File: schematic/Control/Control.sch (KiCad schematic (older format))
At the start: 0 parts

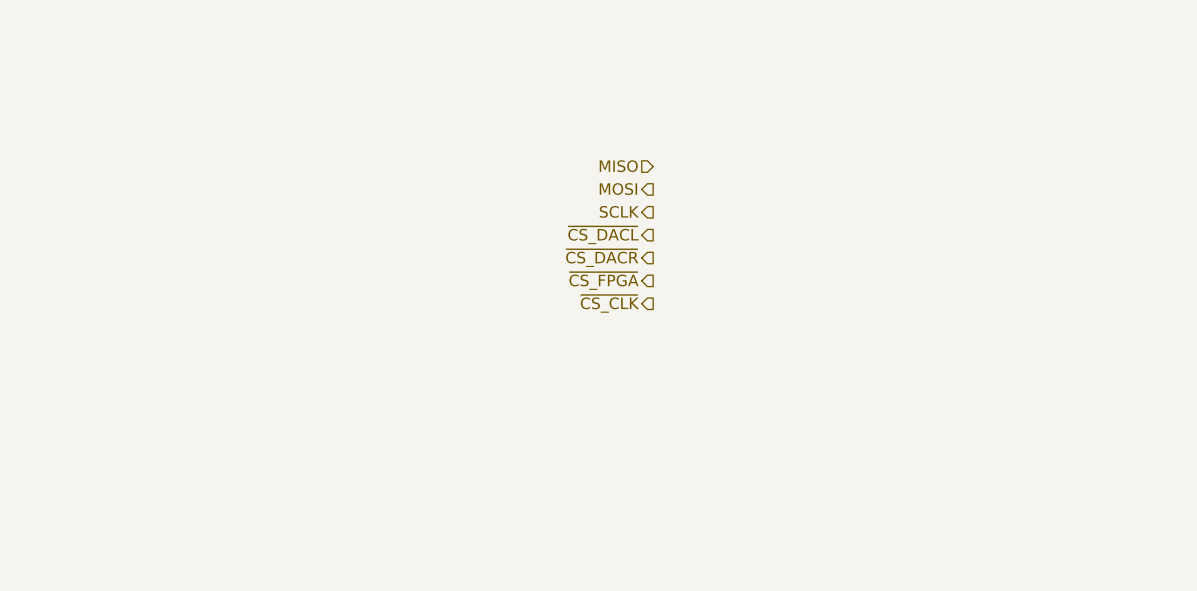
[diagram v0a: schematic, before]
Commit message: Control board diagram complete at high level - Clock, USB, Control, Power and IO done. Remaining is FPGA pin assignment which will be done later to optimize board layout.
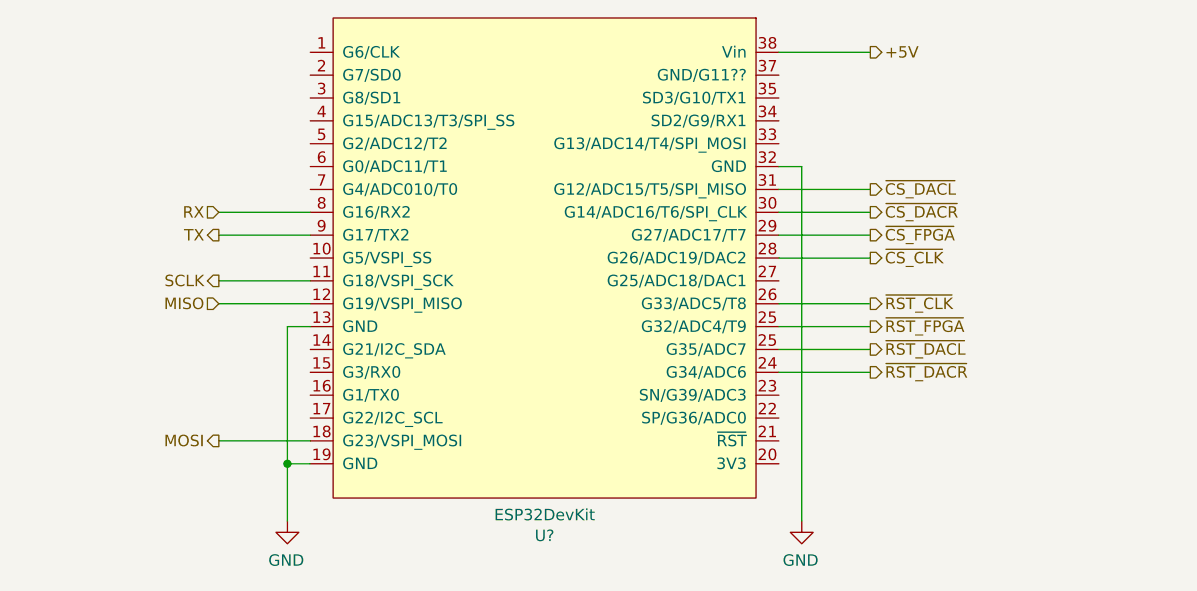
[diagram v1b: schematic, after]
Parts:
- added U?: ESP32DevKit, Zmei_Footprints:ESP32DevKit, symbol Zmei_elements:ESP32DevKit
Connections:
- net MISO: now also U?.12 (G19/VSPI_MISO)
- net MOSI: now also U?.18 (G23/VSPI_MOSI)
- net SCLK: now also U?.11 (G18/VSPI_SCK)
- net ~CS_CLK~: now also U?.28 (G26/ADC19/DAC2)
- net ~CS_DACL~: now also U?.31 (G12/ADC15/T5/SPI_MISO)
- net ~CS_DACR~: now also U?.30 (G14/ADC16/T6/SPI_CLK)
- net ~CS_FPGA~: now also U?.29 (G27/ADC17/T7)
- new net +5V: U?.38 (Vin)
- new net GND: U?.13 (GND), U?.19 (GND), U?.32 (GND)
- new net RX: U?.8 (G16/RX2)
- new net TX: U?.9 (G17/TX2)
- new net ~RST_CLK~: U?.26 (G33/ADC5/T8)
- new net ~RST_DACL~: U?.25 (G35/ADC7)
- new net ~RST_DACR~: U?.24 (G34/ADC6)
- new net ~RST_FPGA~: U?.25 (G35/ADC7)
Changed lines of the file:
@@
 EESchema Schematic File Version 4
-LIBS:DeWille-cache
 EELAYER 30 0
 EELAYER END
 $Descr A4 11693 8268
 encoding utf-8
-Sheet 4 7
+Sheet 3 5
 Title ""
 Date ""
@@
 Comment4 ""
 $EndDescr
-Text HLabel 6550 3600 0    50   Input ~ 0
+Text HLabel 7500 3700 2    50   Output ~ 0
+~CS_DACL~
+Text HLabel 7500 3800 2    50   Output ~ 0
+~CS_DACR~
+Text HLabel 7500 3900 2    50   Output ~ 0
+~CS_FPGA~
+Text HLabel 7500 4000 2    50   Output ~ 0
+~CS_CLK~
+Text HLabel 7500 4200 2    50   Output ~ 0
+~RST_CLK~
+Text HLabel 7500 4300 2    50   Output ~ 0
+~RST_FPGA~
+Text HLabel 7500 4400 2    50   Output ~ 0
+~RST_DACL~
+Text HLabel 7500 4500 2    50   Output ~ 0
+~RST_DACR~
+Text HLabel 4650 3900 0    50   Output ~ 0
+TX
+Text HLabel 4650 3800 0    50   Input ~ 0
+RX
+Text HLabel 4650 4100 0    50   Output ~ 0
+SCLK
+Text HLabel 4650 4800 0    50   Output ~ 0
+MOSI
+Text HLabel 4650 4200 0    50   Input ~ 0
 MISO
-Text HLabel 6550 3700 0    50   Output ~ 0
-MOSI
-Text HLabel 6550 3800 0    50   Output ~ 0
-SCLK
-Text HLabel 6550 3900 0    50   Output ~ 0
-~CS_DACL~
-Text HLabel 6550 4000 0    50   Output ~ 0
-~CS_DACR~
-Text HLabel 6550 4100 0    50   Output ~ 0
-~CS_FPGA~
-Text HLabel 6550 4200 0    50   Output ~ 0
-~CS_CLK~
+Wire Wire Line
+	5050 4100 4650 4100
+Wire Wire Line
+	5050 4200 4650 4200
+Wire Wire Line
+	5050 4800 4650 4800
+Wire Wire Line
+	4650 3800 5050 3800
+Wire Wire Line
+	5050 3900 4650 3900
+$Comp
+L Zmei_elements:ESP32DevKit U?
+U 1 1 5E265BB1
+P 6050 4100
+F 0 "U?" H 6025 5215 50  0000 C CNN
+F 1 "ESP32DevKit" H 6025 5124 50  0000 C CNN
+F 2 "Zmei_Footprints:ESP32DevKit" H 5950 2850 50  0001 C CNN
+F 3 "https://www.aliexpress.com/item/32992390199.html?spm=a2g0s.9042311.0.0.23c84c4dkfKnQl" H 5150 5400 50  0001 C CNN
+	1    6050 4100
+	-1   0    0    1
+$EndComp
+Wire Wire Line
+	7100 3600 7200 3600
+$Comp
+L power:GND #PWR?
+U 1 1 5E26E263
+P 7200 5150
+AR Path="/5DD2C0D9/5E26E263" Ref="#PWR?"  Part="1"
+AR Path="/5E26E263" Ref="#PWR?"  Part="1"
+AR Path="/5DDEE9E3/5E26E263" Ref="#PWR?"  Part="1"
+F 0 "#PWR?" H 7200 4900 50  0001 C CNN
+F 1 "GND" H 7205 4977 50  0000 C CNN
+F 2 "" H 7200 5150 50  0001 C CNN
+F 3 "" H 7200 5150 50  0001 C CNN
+	1    7200 5150
+	-1   0    0    -1
+$EndComp
+$Comp
+L power:GND #PWR?
+U 1 1 5E26E6FE
+P 4950 5150
+AR Path="/5DD2C0D9/5E26E6FE" Ref="#PWR?"  Part="1"
+AR Path="/5E26E6FE" Ref="#PWR?"  Part="1"
+AR Path="/5DDEE9E3/5E26E6FE" Ref="#PWR?"  Part="1"
+F 0 "#PWR?" H 4950 4900 50  0001 C CNN
+F 1 "GND" H 4955 4977 50  0000 C CNN
+F 2 "" H 4950 5150 50  0001 C CNN
+F 3 "" H 4950 5150 50  0001 C CNN
+	1    4950 5150
+	-1   0    0    -1
+$EndComp
+Wire Wire Line
+	4950 4300 5050 4300
+Wire Wire Line
+	5050 4900 4950 4900
+Wire Wire Line
+	4950 4900 4950 4300
+Wire Wire Line
+	7200 5150 7200 3600
+Wire Wire Line
+	4950 4900 4950 5150
+Connection ~ 4950 4900
+Text HLabel 7500 3100 2    50   Output ~ 0
++5V
+Wire Wire Line
+	7500 3100 7100 3100
+Wire Wire Line
+	7500 3700 7100 3700
+Wire Wire Line
+	7500 3800 7100 3800
+Wire Wire Line
+	7500 3900 7100 3900
+Wire Wire Line
+	7500 4000 7100 4000
+Wire Wire Line
+	7500 4200 7100 4200
+Wire Wire Line
+	7500 4300 7100 4300
+Wire Wire Line
+	7500 4400 7100 4400
+Wire Wire Line
+	7500 4500 7100 4500
 $EndSCHEMATC

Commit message: Provision for SPI Slave FPGA bitstream download. Switch RAM from x16 to x8 one.
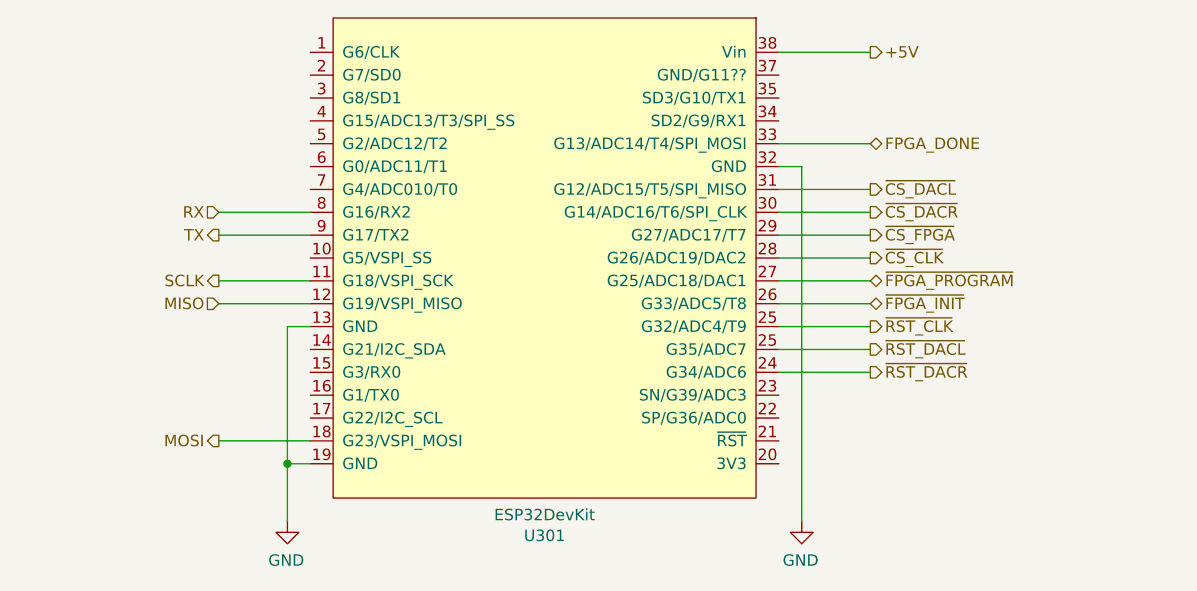
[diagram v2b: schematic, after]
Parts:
- gave numbers to parts that had none: 1
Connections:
- net ~RST_FPGA~ is gone; now on net ~RST_DACL~: U301.25 (G35/ADC7)
- net ~RST_CLK~: now also U301.25 (G35/ADC7); no longer U301.26 (G33/ADC5/T8)
- net ~FPGA_PROGRAM~: now reaches U301.27 (G25/ADC18/DAC1)
- net FPGA_DONE: now reaches U301.33 (G13/ADC14/T4/SPI_MOSI)
- new net ~FPGA_INIT~: U301.26 (G33/ADC5/T8)
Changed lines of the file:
@@
 EESchema Schematic File Version 4
+LIBS:DeWille_Control-cache
 EELAYER 30 0
 EELAYER END
@@
 Text HLabel 7500 4000 2    50   Output ~ 0
 ~CS_CLK~
-Text HLabel 7500 4200 2    50   Output ~ 0
+Text HLabel 7500 4300 2    50   Output ~ 0
 ~RST_CLK~
-Text HLabel 7500 4300 2    50   Output ~ 0
-~RST_FPGA~
 Text HLabel 7500 4400 2    50   Output ~ 0
 ~RST_DACL~
@@
 	5050 3900 4650 3900
 $Comp
-L Zmei_elements:ESP32DevKit U?
+L Zmei_elements:ESP32DevKit U301
 U 1 1 5E265BB1
 P 6050 4100
-F 0 "U?" H 6025 5215 50  0000 C CNN
+F 0 "U301" H 6025 5215 50  0000 C CNN
 F 1 "ESP32DevKit" H 6025 5124 50  0000 C CNN
 F 2 "Zmei_Footprints:ESP32DevKit" H 5950 2850 50  0001 C CNN
@@
 AR Path="/5DD2C0D9/5E26E263" Ref="#PWR?"  Part="1"
 AR Path="/5E26E263" Ref="#PWR?"  Part="1"
-AR Path="/5DDEE9E3/5E26E263" Ref="#PWR?"  Part="1"
-F 0 "#PWR?" H 7200 4900 50  0001 C CNN
+AR Path="/5DDEE9E3/5E26E263" Ref="#PWR0302"  Part="1"
+F 0 "#PWR0302" H 7200 4900 50  0001 C CNN
 F 1 "GND" H 7205 4977 50  0000 C CNN
 F 2 "" H 7200 5150 50  0001 C CNN
@@
 AR Path="/5DD2C0D9/5E26E6FE" Ref="#PWR?"  Part="1"
 AR Path="/5E26E6FE" Ref="#PWR?"  Part="1"
-AR Path="/5DDEE9E3/5E26E6FE" Ref="#PWR?"  Part="1"
-F 0 "#PWR?" H 4950 4900 50  0001 C CNN
+AR Path="/5DDEE9E3/5E26E6FE" Ref="#PWR0301"  Part="1"
+F 0 "#PWR0301" H 4950 4900 50  0001 C CNN
 F 1 "GND" H 4955 4977 50  0000 C CNN
 F 2 "" H 4950 5150 50  0001 C CNN
@@
 Wire Wire Line
 	7500 4500 7100 4500
+Wire Wire Line
+	7100 4100 7500 4100
+Text HLabel 7500 4100 2    50   BiDi ~ 0
+~FPGA_PROGRAM~
+Text HLabel 7500 4200 2    50   BiDi ~ 0
+~FPGA_INIT~
+Text HLabel 7500 3500 2    50   BiDi ~ 0
+FPGA_DONE
+Wire Wire Line
+	7100 3500 7500 3500
 $EndSCHEMATC

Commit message: Interim commit
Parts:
- added R301, R302: 10k, Resistor_SMD:R_0603_1608Metric, symbol Device:R
- added SW301: SW_DIP_x02, Package_DIP:DIP-4_W7.62mm, symbol Switch:SW_DIP_x02
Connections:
- net GND: now also SW301.1, SW301.2
- net ~RST_DACL~: now also U301.15 (G3/RX0); no longer U301.25 (G35/ADC7)
- net ~RST_DACR~: now also U301.16 (G1/TX0); no longer U301.24 (G34/ADC6)
- net ~RST_FPGA~: now reaches U301.14 (G21/I2C_SDA)
- net at U301.20 (3V3): now also R301.2, R302.2
- net at U301.22 (SP/G36/ADC0): now also R301.1, SW301.3
- net at U301.23 (SN/G39/ADC3): now also R302.1, SW301.4
- net LED1: now reaches U301.5 (G2/ADC12/T2)
- net LED2: now reaches U301.6 (G0/ADC11/T1)
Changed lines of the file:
@@
 Text HLabel 7500 4300 2    50   Output ~ 0
 ~RST_CLK~
-Text HLabel 7500 4400 2    50   Output ~ 0
+Text HLabel 4650 4500 0    50   Output ~ 0
 ~RST_DACL~
-Text HLabel 7500 4500 2    50   Output ~ 0
+Text HLabel 4650 4600 0    50   Output ~ 0
 ~RST_DACR~
 Text HLabel 4650 3900 0    50   Output ~ 0
@@
 	7500 4300 7100 4300
 Wire Wire Line
-	7500 4400 7100 4400
-Wire Wire Line
-	7500 4500 7100 4500
+	4650 4500 5050 4500
+Wire Wire Line
+	4650 4600 5050 4600
 Wire Wire Line
 	7100 4100 7500 4100
@@
 Wire Wire Line
 	7100 3500 7500 3500
+Text HLabel 4650 3500 0    50   Output ~ 0
+LED1
+Text HLabel 4650 3600 0    50   Output ~ 0
+LED2
+Wire Wire Line
+	5050 3600 4650 3600
+Wire Wire Line
+	4650 3500 5050 3500
+$Comp
+L Switch:SW_DIP_x02 SW301
+U 1 1 60548328
+P 8350 4700
+F 0 "SW301" H 8350 5067 50  0000 C CNN
+F 1 "SW_DIP_x02" H 8350 4976 50  0000 C CNN
+F 2 "Package_DIP:DIP-4_W7.62mm" H 8350 4700 50  0001 C CNN
+F 3 "~" H 8350 4700 50  0001 C CNN
+	1    8350 4700
+	-1   0    0    -1
+$EndComp
+Wire Wire Line
+	7100 4600 7800 4600
+Wire Wire Line
+	8050 4700 7550 4700
+Wire Wire Line
+	8650 4600 8750 4600
+Wire Wire Line
+	8750 4600 8750 4700
+Wire Wire Line
+	8650 4700 8750 4700
+Connection ~ 8750 4700
+Wire Wire Line
+	8750 4700 8750 4800
+$Comp
+L power:GND #PWR?
+U 1 1 6054AF43
+P 8750 4800
+AR Path="/5DD2C0D9/6054AF43" Ref="#PWR?"  Part="1"
+AR Path="/6054AF43" Ref="#PWR?"  Part="1"
+AR Path="/5DDEE9E3/6054AF43" Ref="#PWR0146"  Part="1"
+F 0 "#PWR0146" H 8750 4550 50  0001 C CNN
+F 1 "GND" H 8755 4627 50  0000 C CNN
+F 2 "" H 8750 4800 50  0001 C CNN
+F 3 "" H 8750 4800 50  0001 C CNN
+	1    8750 4800
+	1    0    0    -1
+$EndComp
+$Comp
+L Device:R R?
+U 1 1 6055116C
+P 7800 4900
+AR Path="/5DBF9B5A/6055116C" Ref="R?"  Part="1"
+AR Path="/5DCC3140/6055116C" Ref="R?"  Part="1"
+AR Path="/5DD2C0D9/6055116C" Ref="R?"  Part="1"
+AR Path="/5DDC09A7/6055116C" Ref="R?"  Part="1"
+AR Path="/6055116C" Ref="R?"  Part="1"
+AR Path="/5DDEE9E3/6055116C" Ref="R302"  Part="1"
+F 0 "R302" H 7600 4900 50  0000 L CNN
+F 1 "10k" H 7600 4800 50  0000 L CNN
+F 2 "Resistor_SMD:R_0603_1608Metric" V 7730 4900 50  0001 C CNN
+F 3 "~" H 7800 4900 50  0001 C CNN
+	1    7800 4900
+	1    0    0    -1
+$EndComp
+$Comp
+L Device:R R?
+U 1 1 60551616
+P 7550 4900
+AR Path="/5DBF9B5A/60551616" Ref="R?"  Part="1"
+AR Path="/5DCC3140/60551616" Ref="R?"  Part="1"
+AR Path="/5DD2C0D9/60551616" Ref="R?"  Part="1"
+AR Path="/5DDC09A7/60551616" Ref="R?"  Part="1"
+AR Path="/60551616" Ref="R?"  Part="1"
+AR Path="/5DDEE9E3/60551616" Ref="R301"  Part="1"
+F 0 "R301" H 7350 4900 50  0000 L CNN
+F 1 "10k" H 7350 4800 50  0000 L CNN
+F 2 "Resistor_SMD:R_0603_1608Metric" V 7480 4900 50  0001 C CNN
+F 3 "~" H 7550 4900 50  0001 C CNN
+	1    7550 4900
+	1    0    0    -1
+$EndComp
+Wire Wire Line
+	7550 4750 7550 4700
+Connection ~ 7550 4700
+Wire Wire Line
+	7550 4700 7100 4700
+Wire Wire Line
+	7800 4750 7800 4600
+Connection ~ 7800 4600
+Wire Wire Line
+	7800 4600 8050 4600
+Wire Wire Line
+	7100 4900 7300 4900
+Wire Wire Line
+	7300 4900 7300 5100
+Wire Wire Line
+	7300 5100 7550 5100
+Wire Wire Line
+	7800 5100 7800 5050
+Wire Wire Line
+	7550 5050 7550 5100
+Connection ~ 7550 5100
+Wire Wire Line
+	7550 5100 7800 5100
+Text HLabel 4650 4400 0    50   Output ~ 0
+~RST_FPGA~
+Wire Wire Line
+	4650 4400 5050 4400
 $EndSCHEMATC

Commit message: Routing complete
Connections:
- wire segments 41 -> 43
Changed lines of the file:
@@
 Comment4 ""
 $EndDescr
-Text HLabel 7500 3700 2    50   Output ~ 0
+Text HLabel 7500 4300 2    50   Output ~ 0
 ~CS_DACL~
+Text HLabel 7500 4100 2    50   Output ~ 0
+~CS_DACR~
+Text HLabel 4650 4500 0    50   Output ~ 0
+~CS_FPGA~
+Text HLabel 7500 3900 2    50   Output ~ 0
+~CS_CLK~
 Text HLabel 7500 3800 2    50   Output ~ 0
-~CS_DACR~
-Text HLabel 7500 3900 2    50   Output ~ 0
-~CS_FPGA~
+~RST_CLK~
+Text HLabel 7500 4200 2    50   Output ~ 0
+~RST_DACL~
 Text HLabel 7500 4000 2    50   Output ~ 0
-~CS_CLK~
-Text HLabel 7500 4300 2    50   Output ~ 0
-~RST_CLK~
-Text HLabel 4650 4500 0    50   Output ~ 0
-~RST_DACL~
-Text HLabel 4650 4600 0    50   Output ~ 0
 ~RST_DACR~
 Text HLabel 4650 3900 0    50   Output ~ 0
@@
 Wire Wire Line
 	7100 4100 7500 4100
-Text HLabel 7500 4100 2    50   BiDi ~ 0
+Text HLabel 4650 4700 0    50   BiDi ~ 0
 ~FPGA_PROGRAM~
-Text HLabel 7500 4200 2    50   BiDi ~ 0
+Text HLabel 4650 4000 0    50   BiDi ~ 0
 ~FPGA_INIT~
-Text HLabel 7500 3500 2    50   BiDi ~ 0
+Text HLabel 4650 4600 0    50   BiDi ~ 0
 FPGA_DONE
 Wire Wire Line
@@
 Wire Wire Line
 	4650 4400 5050 4400
+Wire Wire Line
+	5050 4700 4650 4700
+Wire Wire Line
+	5050 4000 4650 4000
 $EndSCHEMATC
